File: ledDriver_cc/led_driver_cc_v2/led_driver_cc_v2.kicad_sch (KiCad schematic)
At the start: 25 parts, among them J1 Conn_01x08_Pin, J3 Conn_01x02_Female, U1 TSR_1-2490, U2 LM3404

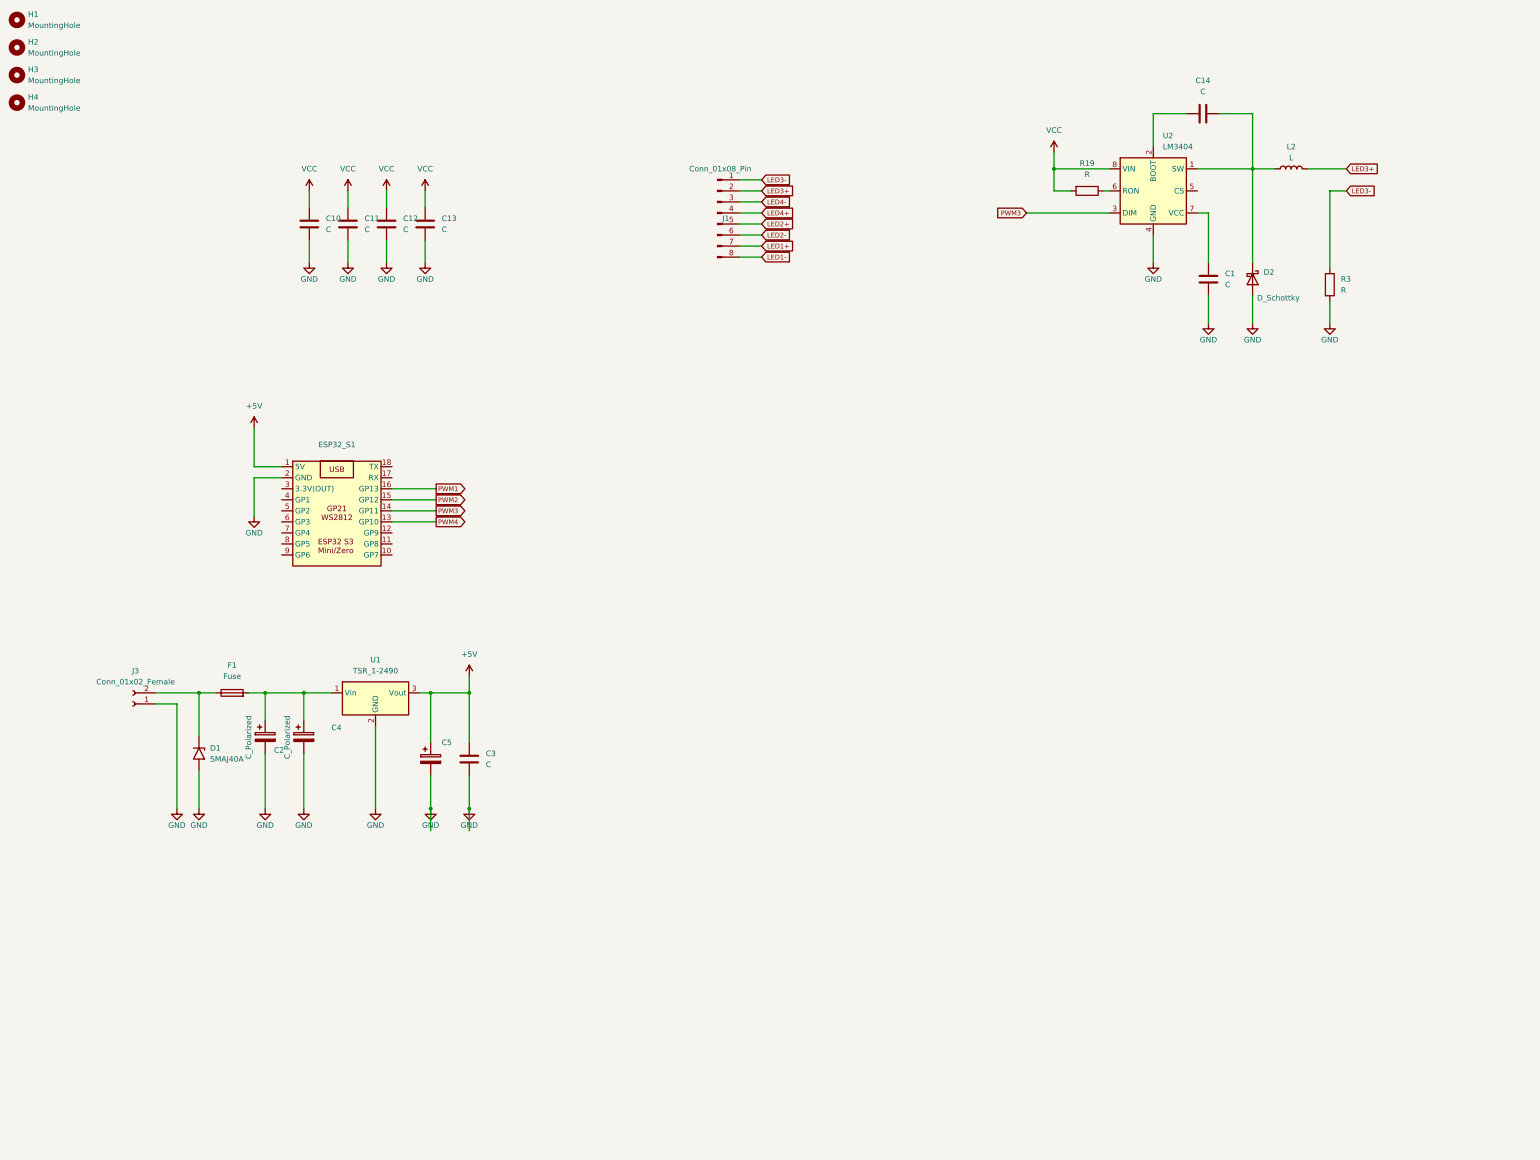
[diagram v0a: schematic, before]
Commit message: add new channels to led driver
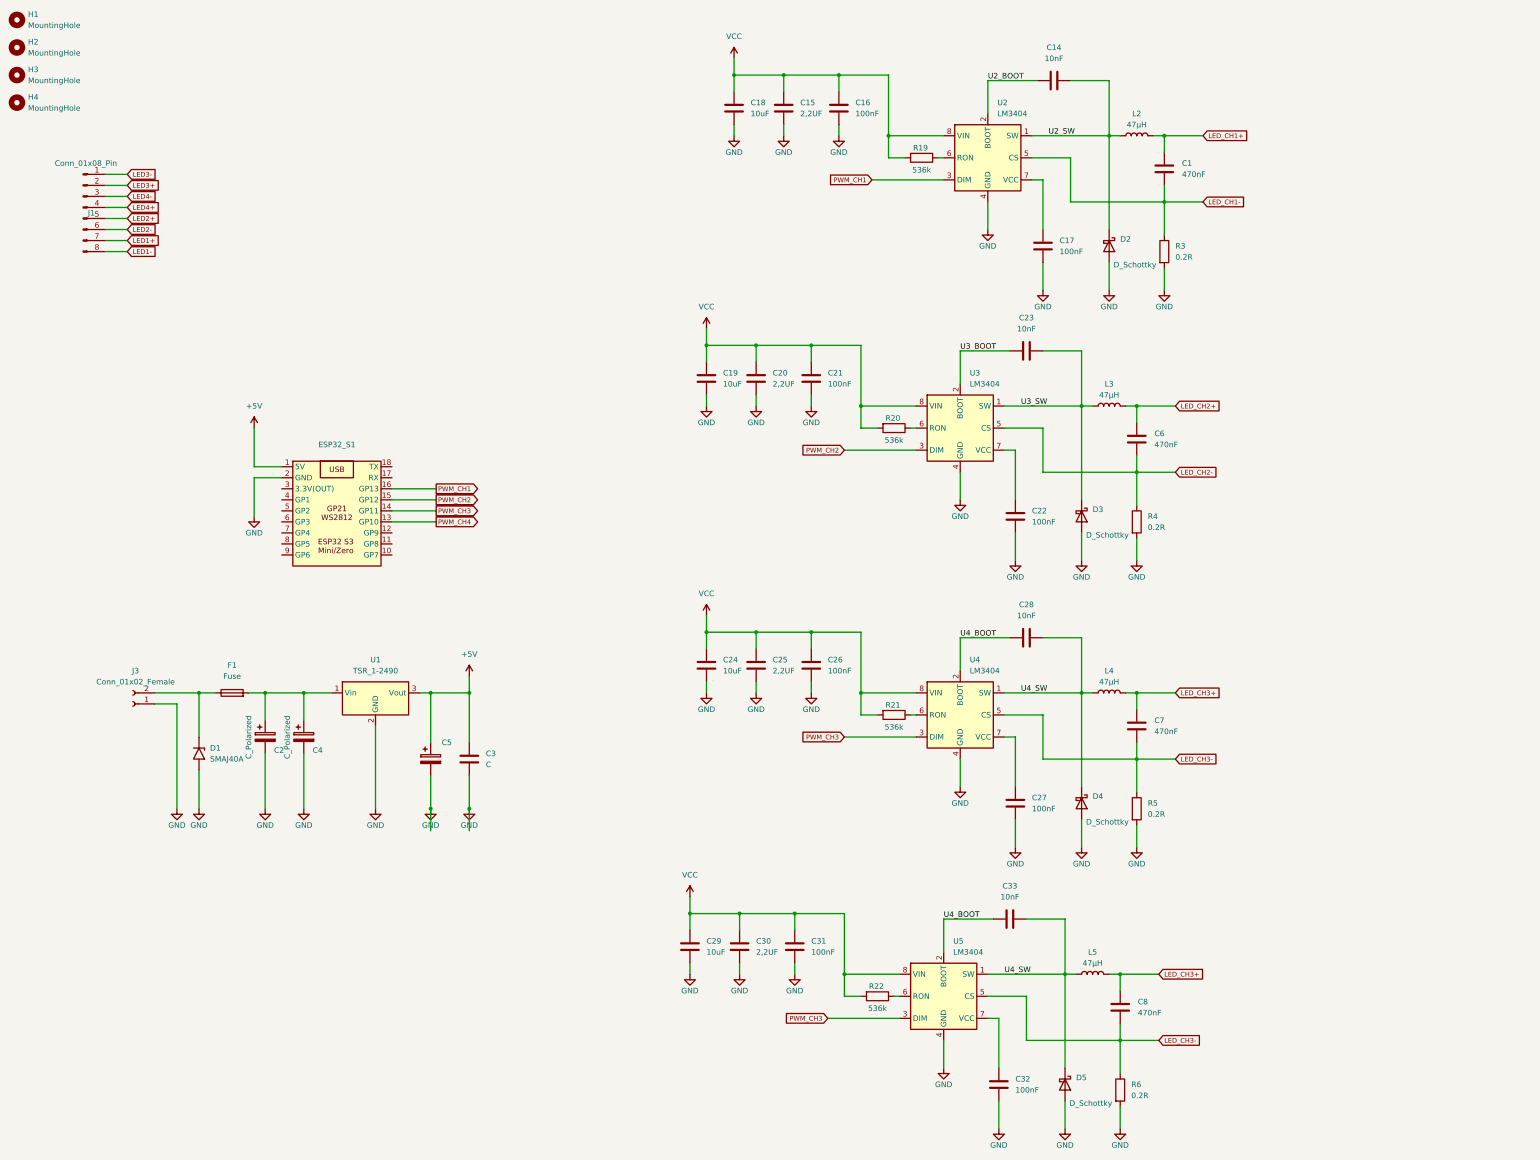
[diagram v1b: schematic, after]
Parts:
- removed C10, C11, C12, C13: C, Capacitor_SMD:C_1210_3225Metric_Pad1.33x2.70mm_HandSolder, symbol Device:C
- added C15, C20, C25, C30: 2,2UF, Capacitor_SMD:C_1206_3216Metric_Pad1.33x1.80mm_HandSolder, symbol Device:C
- added C16, C17, C21, C22, C26, C27, C31, C32: 100nF, Capacitor_SMD:C_1206_3216Metric_Pad1.33x1.80mm_HandSolder, symbol Device:C
- added C18, C19, C24, C29: 10uF, Capacitor_SMD:C_1210_3225Metric_Pad1.33x2.70mm_HandSolder, symbol Device:C
- added C23, C28, C33: 10nF, Capacitor_SMD:C_1206_3216Metric_Pad1.33x1.80mm_HandSolder, symbol Device:C
- added C6, C7, C8: 470nF, Capacitor_SMD:C_1210_3225Metric_Pad1.33x2.70mm_HandSolder, symbol Device:C
- added D3, D4, D5: D_Schottky, Diode_SMD:D_SMB, symbol Device:D_Schottky
- added L3, L4, L5: 47µH, Inductor_SMD:L_TDK_SLF10145, symbol Device:L
- added R20, R21, R22: 536k, Resistor_SMD:R_0805_2012Metric_Pad1.20x1.40mm_HandSolder, symbol Device:R
- added R4, R5, R6: 0.2R, Resistor_SMD:R_2512_6332Metric_Pad1.40x3.35mm_HandSolder, symbol Device:R
- added U3, U4, U5: LM3404, Package_SO:SOIC-8_3.9x4.9mm_P1.27mm, symbol custom_symbols:LM3404
- C1: value C -> 470nF
- C14: value C -> 10nF
- C2, C4: footprint Capacitor_THT:CP_Radial_D13.0mm_P5.00mm -> Capacitor_SMD:CP_Elec_10x10
- L2: value L -> 47µH
- R19: value R -> 536k
- R3: value R -> 0.2R
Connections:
- net GND: now also C15.1, C16.1, C17.1, C18.1, C19.1, C20.1, C21.1, C22.1, C24.1, C25.1, C26.1, C27.1, C29.1, C30.1, C31.1, C32.1, D3.2 (A), D4.2 (A), D5.2 (A), R4.2, R5.2, R6.2, U3.4 (GND), U4.4 (GND), U5.4 (GND); no longer C1.2
- net LED3+: no longer L2.2
- net LED3-: no longer R3.1
- net VCC: now also C15.2, C16.2, C18.2, C19.2, C20.2, C21.2, C24.2, C25.2, C26.2, C29.2, C30.2, C31.2, R20.2, R21.2, R22.2, U3.8 (VIN), U4.8 (VIN), U5.8 (VIN)
- net U2_BOOT: now reaches C14.1, U2.2 (BOOT)
- net U2_SW: now reaches C14.2, D2.1 (K), L2.1, U2.1 (SW)
- net at U2.7 (VCC): now also C17.2; no longer C1.1
- net LED_CH1-: now reaches U2.5 (CS)
- net LED_CH1-: now also C1.2, R3.1
- net PWM1 renamed PWM_CH1
- net PWM_CH1: now also U2.3 (DIM)
- net PWM2 renamed PWM_CH2
- net PWM_CH2: now also U3.3 (DIM)
- net PWM3 renamed PWM_CH3
- net PWM_CH3: now also U4.3 (DIM), U5.3 (DIM); no longer U2.3 (DIM)
- net PWM4 renamed PWM_CH4
- new net: C22.2, U3.7 (VCC)
- new net: R21.1, U4.6 (RON)
- new net: R20.1, U3.6 (RON)
- new net: R22.1, U5.6 (RON)
- new net: C32.2, U5.7 (VCC)
- new net: C27.2, U4.7 (VCC)
- new net LED_CH1+: C1.1, L2.2
- new net LED_CH2+: C6.1, L3.2
- new net LED_CH2-: C6.2, R4.1, U3.5 (CS)
- new net LED_CH3+: C7.1, C8.1, L4.2, L5.2
- new net LED_CH3-: C7.2, C8.2, R5.1, R6.1, U4.5 (CS), U5.5 (CS)
- new net U3_BOOT: C23.1, U3.2 (BOOT)
- new net U3_SW: C23.2, D3.1 (K), L3.1, U3.1 (SW)
- new net U4_BOOT: C28.1, C33.1, U4.2 (BOOT), U5.2 (BOOT)
- new net U4_SW: C28.2, C33.2, D4.1 (K), D5.1 (K), L4.1, L5.1, U4.1 (SW), U5.1 (SW)
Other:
- moved on the sheet: C1, C14, D2, J1, L2, R19, R3, U2

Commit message: new channel arrangement
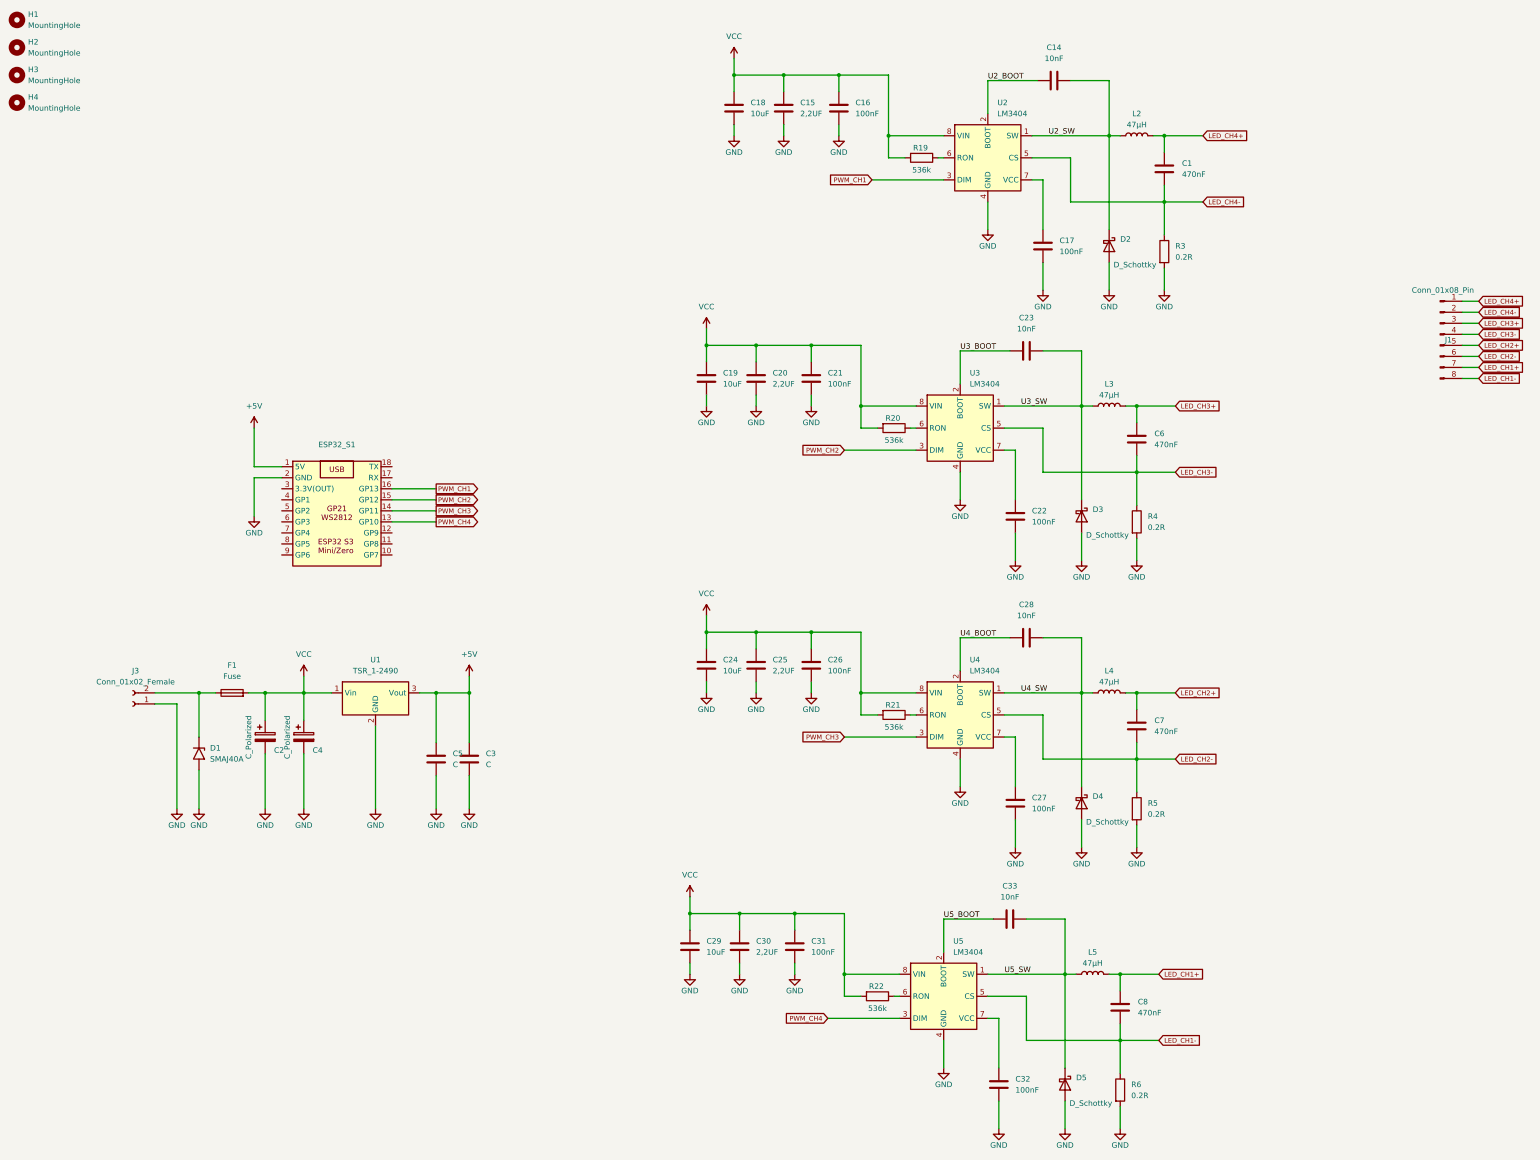
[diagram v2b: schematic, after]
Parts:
- removed C5: C_Polarized, Capacitor_THT:CP_Radial_D6.3mm_P2.50mm, symbol Device:C_Polarized
- added C5: C, Capacitor_SMD:C_1210_3225Metric_Pad1.33x2.70mm_HandSolder, symbol Device:C
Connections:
- net LED1+ is gone; now on net LED_CH1+: J1.7 (Pin_7)
- net LED1- is gone; now on net LED_CH1-: J1.8 (Pin_8)
- net LED2+ is gone; now on net LED_CH2+: J1.5 (Pin_5)
- net LED2- is gone; now on net LED_CH2-: J1.6 (Pin_6)
- net LED4+ is gone; now on net LED_CH3-: J1.4 (Pin_4)
- net LED4- is gone; now on net LED_CH3+: J1.3 (Pin_3)
- net +5V: now also C5.1
- net GND: now also C5.2
- net LED_CH1+: now also C8.1, L5.2; no longer C1.1, L2.2
- net LED_CH1-: now also C8.2, R6.1, U5.5 (CS); no longer C1.2, R3.1, U2.5 (CS)
- net LED_CH2+: now also C7.1, L4.2; no longer C6.1, L3.2
- net LED_CH2-: now also C7.2, R5.1, U4.5 (CS); no longer C6.2, R4.1, U3.5 (CS)
- net LED_CH3+: now also C6.1, L3.2; no longer C7.1, C8.1, L4.2, L5.2
- net LED_CH3-: now also C6.2, R4.1, U3.5 (CS); no longer C7.2, C8.2, R5.1, R6.1, U4.5 (CS), U5.5 (CS)
- net PWM_CH3: no longer U5.3 (DIM)
- net PWM_CH4: now also U5.3 (DIM)
- net U4_BOOT: no longer C33.1, U5.2 (BOOT)
- net U4_SW: no longer C33.2, D5.1 (K), L5.1, U5.1 (SW)
- net VCC: now also C2.1, C4.1, F1.2, U1.1 (Vin)
- net LED3+ renamed LED_CH4-
- net LED_CH4-: now also C1.2, R3.1, U2.5 (CS)
- net LED3- renamed LED_CH4+
- net LED_CH4+: now also C1.1, L2.2
- new net U5_BOOT: C33.1, U5.2 (BOOT)
- new net U5_SW: C33.2, D5.1 (K), L5.1, U5.1 (SW)
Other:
- moved on the sheet: J1
